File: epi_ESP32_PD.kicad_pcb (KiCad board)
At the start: 4 copper layers, 12.7 x 49.6 mm, 62 parts, among them J1 Conn_01x08, J2 USB_C_Receptacle_USB2.0, J3 Conn_01x08, J4 Conn_01x02, J6 Conn_Coaxial_Small, J7 Conn_02x03, J8 Conn_01x03, Q1 Q_PMOS_GDS, Q2 Q_NMOS_GDS, Q3 Q_NMOS_GDS, Q4 Q_NMOS_GDS, Q5 Q_NMOS_GDS, Q6 Q_NMOS_GDS, SW1 SW_MEC_5G, SW2 SW_MEC_5G, U1 ESP32-C3, U2 MIC5219-3.3YM5, U5 AP63205WU, Y1 Crystal

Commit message: made it pretty
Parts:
- removed DRILL1, DRILL2: NPTH, DIY:NPTH
- added JP4: Jumper, Jumper:SolderJumper-2_P1.3mm_Open_RoundedPad1.0x1.5mm, B.Cu at (103.9, 55.1)
- J2: footprint diy:USB-C MC-314C-4P16_V2 (2023_01_13 17_48_46 UTC) -> Connector_USB:USB_C_Receptacle_G-Switch_GT-USB-7010ASV
- moved JP3 1.65 mm to (101.9, 44.4), turned to 180 degrees
- moved JP2 0.89 mm to (101.9, 47.5), turned to 0 degrees
- moved J4 0.51 mm to (108.3, 48.9)
- moved R13 0.41 mm to (109.0, 79.3), turned to -90 degrees
- moved JP1 0.40 mm to (101.9, 50.6), turned to 0 degrees
- moved SW1 0.30 mm to (102.1, 61.5)
- moved R11 0.22 mm to (106.1, 75.0)
- moved C7 0.20 mm to (104.9, 68.5)
- moved J2 0.17 mm to (104.2, 36.4)
- moved C14 0.10 mm to (106.3, 53.1)
- moved R7 0.10 mm to (100.0, 45.4)
- moved C8 0.10 mm to (100.0, 43.2)
- moved R15 0.10 mm to (100.0, 46.4)
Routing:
- net +5V: track 60.0 -> 64.9 mm
- net Net-(JP2-B): track 12.7 -> 9.06 mm, vias 2 -> 1
- net IO2: track 23.4 -> 20.7 mm
- net Net-(JP1-B): track 14.5 -> 12.7 mm, vias 2 -> 1
- net Net-(JP3-A): track 3.20 -> 4.95 mm
- net D-: track 32.3 -> 33.7 mm
- net VIN: track 26.2 -> 26.9 mm
- net IO6: track 25.1 -> 24.5 mm
- net GND: vias 20 -> 24
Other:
- board size 12.7 x 49.6 mm -> 12.7 x 49.9 mm
- board text added: "20"
- board text added: "21"
- board text added: "3,3V"
- board text added: "5V"
- board text added: "B"
- board text added: "GND"
- board text added: "IO2-5V"
- board text added: "IO3-5V"
- board text added: "VOUT"
- board text added: "W"
- board text removed: "10"
- board text removed: "3,3v"
- board text removed: "RX/20"
- board text removed: "TX/21"

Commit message: finishing touches
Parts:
- removed C8: 1µF, Capacitor_SMD:C_0805_2012Metric
- added D1: D_Small, Diode_SMD:D_SOD-128, F.Cu at (104.7, 44.2)
- added REF**: Fiducial_0.5mm_Mask1.5mm, Fiducial:Fiducial_0.5mm_Mask1.5mm, F.Cu at (100.3, 36.5)
- J4: value Conn_01x02 -> Conn_01x01; footprint Connector_PinHeader_2.54mm:PinHeader_1x02_P2.54mm_Vertical -> TestPoint:TestPoint_Pad_3.0x3.0mm
- moved RV2 7.02 mm to (102.3, 44.3)
- moved RV3 7.02 mm to (102.3, 42.4), turned to -90 degrees
- moved R3 7.01 mm to (102.3, 46.2)
- moved U3 6.98 mm to (98.1, 44.3)
- moved J4 6.44 mm to (101.9, 49.0), turned to 180 degrees
- moved R1 4.30 mm to (103.9, 47.9)
- moved R8 4.30 mm to (103.9, 48.9)
- moved JP4 4.16 mm to (100.0, 53.7)
- moved J8 3.99 mm to (94.0, 71.1)
- moved Q1 3.94 mm to (103.9, 72.6)
- moved Q3 3.94 mm to (96.9, 72.6)
- moved Q5 3.94 mm to (100.4, 72.6)
- moved R12 3.94 mm to (95.4, 81.5)
- moved R13 3.94 mm to (105.1, 79.7), turned to 90 degrees
- moved R4 3.94 mm to (103.3, 70.0)
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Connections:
- J2 pad A4: VIN -> /PD
- J2 pad A9: VIN -> /PD
- J2 pad B4: VIN -> /PD
- J2 pad B9: VIN -> /PD
- JP1 pad 1: VIN -> +5V
- JP2 pad 1: VIN -> +5V
- JP3 pad 2: VIN -> +5V
- R1 pad 1: Net-(U3-VDD) -> +5V
- R1 pad 2: VIN -> /PD
- R7 pad 1: VIN -> /PD
- U3 pad 1: Net-(U3-VDD) -> +5V
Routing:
- net VIN: track 26.9 -> 6.54 mm, vias 9 -> 5
- net /PD: track 0.00 -> 19.6 mm, vias 0 -> 7
- net +5V: track 64.9 -> 81.4 mm
- net Net-(J2-CC1): track 5.30 -> 13.0 mm
- net EN: track 31.6 -> 26.0 mm
- net Net-(JP3-A): track 4.95 -> 9.07 mm, vias 1 -> 2
- net GND: track 0.00 -> 3.85 mm
- net D-: track 33.7 -> 30.7 mm, vias 3 -> 2
- net Net-(J2-CC2): track 2.05 -> 4.62 mm
- net D+: track 35.1 -> 33.2 mm, vias 3 -> 2
- net Net-(U3-VDD): track 1.82 -> 0.00 mm
- net Net-(JP2-B): track 9.06 -> 7.66 mm
- net +3.3V: track 28.5 -> 29.8 mm, vias 8 -> 9
- net Net-(U3-VBUS): track 3.75 -> 4.48 mm
- net IO2: track 20.7 -> 21.4 mm
- added copper zone on B.Cu, net /PD
- added copper zone on F.Cu, net /PD
- added copper zone on In2.Cu, net /PD
- removed copper zone on In2.Cu, net VIN
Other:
- board text added: "5V only"
- board text added: "IO0"

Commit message: little fix
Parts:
- added C8: 1µF, Capacitor_SMD:C_0402_1005Metric, F.Cu at (101.5, 48.1)
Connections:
- JP1 pad 1: +5V -> +3.3V
- JP2 pad 1: +5V -> +3.3V
- JP3 pad 2: +5V -> +3.3V
- R1 pad 1: +5V -> +3.3V
- U3 pad 1: +5V -> +3.3V
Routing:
- net +5V: track 81.4 -> 63.5 mm
- net +3.3V: track 29.8 -> 43.6 mm, vias 9 -> 11
- net GND: track 3.85 -> 4.58 mm

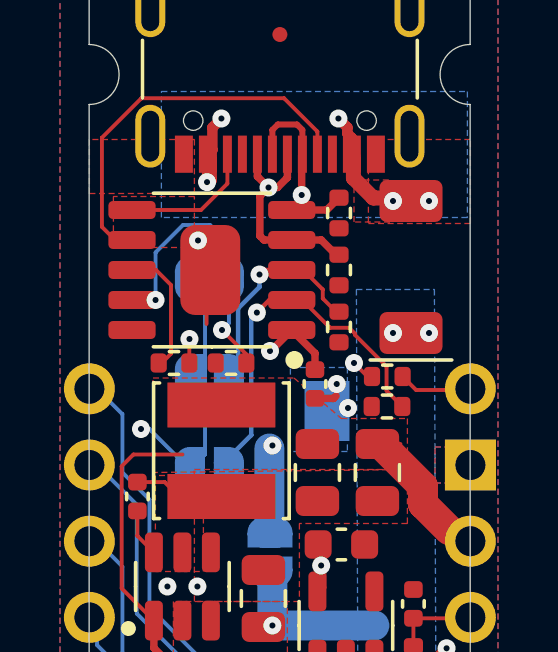
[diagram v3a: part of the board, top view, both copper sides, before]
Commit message: added a couple debugging jumpers
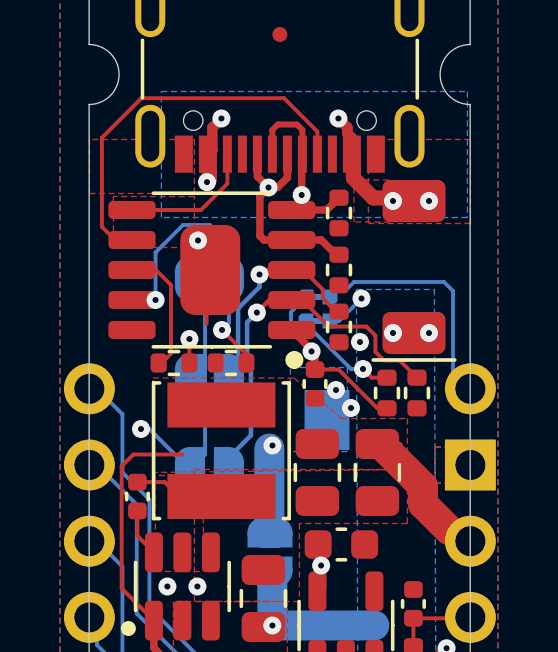
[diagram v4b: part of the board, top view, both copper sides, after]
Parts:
- added JP5: Jumper, Jumper:SolderJumper-2_P1.3mm_Bridged_RoundedPad1.0x1.5mm, B.Cu at (101.6, 46.0)
- added JP6: Jumper, Jumper:SolderJumper-2_P1.3mm_Bridged_RoundedPad1.0x1.5mm, B.Cu at (101.6, 45.2)
- moved R8 1.10 mm to (104.9, 48.4), turned to 90 degrees
- moved R1 0.55 mm to (103.9, 48.4), turned to 90 degrees
- moved J4 0.30 mm to (101.9, 49.3)
- moved D1 0.10 mm to (104.8, 44.2)
- turned C8 to -90 degrees
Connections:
- C8 pad 1: GND -> Net-(JP6-B)
- C8 pad 2: +3.3V -> GND
- R1 pad 1: +3.3V -> Net-(JP6-B)
- R1 pad 2: /PD -> Net-(JP5-A)
- U3 pad 1: +3.3V -> Net-(JP6-B)
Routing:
- net Net-(JP6-B): track 0.00 -> 7.08 mm, vias 0 -> 1
- net Net-(JP5-A): track 0.00 -> 3.54 mm, vias 0 -> 1
- net +3.3V: track 43.6 -> 46.6 mm, vias 11 -> 10
- net /PD: track 19.6 -> 18.0 mm
- net GND: track 4.58 -> 3.85 mm, vias 24 -> 25

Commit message: mix
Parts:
- added D2: D_Zener, Diode_SMD:D_SOD-323, B.Cu at (102.0, 43.2)
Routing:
- net Net-(D2-K): track 7.08 -> 9.18 mm
- net IO2_5V: track 15.3 -> 15.8 mm
- net GND: vias 25 -> 30
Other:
- board size 12.7 x 49.9 mm -> 22.7 x 54.9 mm

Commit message: revision
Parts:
- removed C12, C5: 1µF, Capacitor_SMD:C_0402_1005Metric
- removed C14: 22µF, Capacitor_SMD:C_0603_1608Metric
- removed C2, C7: 100nF, Capacitor_SMD:C_0402_1005Metric
- removed C3, C4, C6: TBD, Capacitor_SMD:C_0402_1005Metric
- removed D2: D_Zener, Diode_SMD:D_SOD-323
- removed J3: Conn_01x08, Connector_PinHeader_2.54mm:PinHeader_1x08_P2.54mm_Vertical
- removed J6: Conn_Coaxial_Small, Connector_Coaxial:U.FL_Molex_MCRF_73412-0110_Vertical
- removed JP5, JP6: Jumper, Jumper:SolderJumper-2_P1.3mm_Bridged_RoundedPad1.0x1.5mm
- removed L1: TBD, Resistor_SMD:R_0402_1005Metric
- removed Q5, Q6: Q_NMOS_GDS, Package_TO_SOT_SMD:SOT-23-3
- removed R2: 22Ω, Resistor_SMD:R_0402_1005Metric
- removed R4, R5: 10K, Resistor_SMD:R_0402_1005Metric
- removed RV2: Varistor, Resistor_SMD:R_0402_1005Metric
- removed SW1: SW_MEC_5G, DIY:R-668048
- removed Y1: Crystal, Crystal:Crystal_SMD_2016-4Pin_2.0x1.6mm
- added J5: Conn_01x09, Connector_PinHeader_2.54mm:PinHeader_1x09_P2.54mm_Vertical, F.Cu at (106.7, 48.3)
- C1: value 100nF -> 1µF
- Q1: value Q_PMOS_GDS -> Q_NMOS_GSD; footprint Package_TO_SOT_SMD:SOT-23-3 -> Package_TO_SOT_SMD:SOT-23
- Q2, Q3, Q4: value Q_NMOS_GDS -> Q_NMOS_GSD; footprint Package_TO_SOT_SMD:SOT-23-3 -> Package_TO_SOT_SMD:SOT-23
- R1: value 1K -> TBD
- R15, R3, R8: value 10K -> 1K
- U1: value ESP32-C3 -> ESP32-C3-MINI-1; footprint Package_DFN_QFN:QFN-32-1EP_5x5mm_P0.5mm_EP3.45x3.45mm -> PCM_Espressif:ESP32-C3-MINI-1
- moved J7 20.1 mm to (104.5, 60.2)
- moved R14 19.7 mm to (96.8, 59.9), turned to 0 degrees
- moved R12 16.9 mm to (98.5, 64.8), turned to 0 degrees
- moved REF** 16.3 mm to (104.8, 44.2)
- moved C1 14.9 mm to (101.5, 54.7)
- moved J8 13.5 mm to (97.8, 84.1), turned to 90 degrees
- moved U1 11.2 mm to (102.5, 76.4), turned to -90 degrees
- moved Q2 11.1 mm to (96.8, 66.2)
- moved R13 11.0 mm to (104.1, 68.7), turned to 180 degrees
- moved Q4 10.5 mm to (103.6, 66.2)
- moved Q3 10.3 mm to (96.8, 62.3), turned to -90 degrees
- moved R11 8.55 mm to (96.8, 68.7)
- moved R10 7.39 mm to (101.9, 68.7), turned to 180 degrees
- moved Q1 7.38 mm to (100.2, 66.2)
- moved REF** 7.37 mm to (98.6, 80.3)
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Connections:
- C8 pad 1: Net-(D2-K) -> +3.3V
- D1 pad 2: /PD -> PD
- J2 pad A4: /PD -> PD
- J2 pad A9: /PD -> PD
- J2 pad B4: /PD -> PD
- J2 pad B9: /PD -> PD
- J7 pad 1: VOUT -> +5V
- J7 pad 3: B -> IO2_5V
- J7 pad 4: IO2_5V -> B
- J7 pad 5: W -> IO3_5V
- J7 pad 6: IO3_5V -> W
- Q1 pad 1: Net-(Q1-G) -> +3.3V
- Q1 pad 2: VOUT -> IO2
- Q1 pad 3: VIN -> IO2_5V
- Q2 pad 1: IO6 -> +3.3V
- Q2 pad 2: B -> IO3
- Q2 pad 3: GND -> IO3_5V
- Q3 pad 1: +3.3V -> IO7
- Q3 pad 2: IO2_5V -> GND
- Q3 pad 3: IO2 -> W
- Q4 pad 1: +3.3V -> IO6
- Q4 pad 2: IO3_5V -> GND
- Q4 pad 3: IO3 -> B
- R1 pad 1: Net-(D2-K) -> +3.3V
- R1 pad 2: Net-(JP5-A) -> PD
- R13 pad 1: IO6 -> GND
- R13 pad 2: +3.3V -> IO6
- R14 pad 1: IO7 -> GND
- R14 pad 2: +3.3V -> IO7
- R7 pad 1: /PD -> PD
- RV3 pad 1: D- -> PD
- U1 pad 1: Net-(U1-LNA_IN) -> GND
- U1 pad 10: IO5 -> unconnected-(U1-NC-Pad10)
- U1 pad 11: +3.3V -> GND
- U1 pad 12: IO6 -> IO0
- U1 pad 13: IO7 -> IO1
- U1 pad 14: IO8 -> GND
- U1 pad 15: BOOT -> unconnected-(U1-NC-Pad15)
- U1 pad 17: +3.3V -> unconnected-(U1-NC-Pad17)
- U1 pad 18: Net-(U1-VDD_SPI/GPIO11) -> IO4
- U1 pad 19: unconnected-(U1-SPIHD/GPIO12-Pad19) -> IO5
- U1 pad 2: +3.3V -> GND
- U1 pad 20: unconnected-(U1-SPIWP/GPIO13-Pad20) -> IO6
- U1 pad 21: unconnected-(U1-SPICS0/GPIO14-Pad21) -> IO7
- U1 pad 22: unconnected-(U1-SPICLK/GPIO15-Pad22) -> IO8
- U1 pad 23: unconnected-(U1-SPID/GPIO16-Pad23) -> BOOT
- U1 pad 25: D- -> unconnected-(U1-NC-Pad25)
- U1 pad 26: D+ -> D-
- U1 pad 27: U0RXD -> D+
- U1 pad 28: U0TXD -> unconnected-(U1-NC-Pad28)
- U1 pad 29: Net-(U1-XTAL_N) -> unconnected-(U1-NC-Pad29)
- U1 pad 30: Net-(U1-XTAL_P) -> U0RXD
- U1 pad 31: +3.3V -> U0TXD
- U1 pad 32: +3.3V -> unconnected-(U1-NC-Pad32)
- U1 pad 33: GND -> unconnected-(U1-NC-Pad33)
- U1 pad 4: IO0 -> unconnected-(U1-NC-Pad4)
- U1 pad 5: IO1 -> IO2
- U1 pad 6: IO2 -> IO3
- U1 pad 7: EN -> unconnected-(U1-NC-Pad7)
- U1 pad 8: IO3 -> EN
- U1 pad 9: IO4 -> unconnected-(U1-NC-Pad9)
- U3 pad 1: Net-(D2-K) -> +3.3V
- U3 pad 4: D+ -> unconnected-(U3-DP-Pad4)
- U3 pad 5: D- -> unconnected-(U3-DM-Pad5)
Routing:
- net +5V: track 63.7 -> 35.5 mm, vias 2 -> 4
- net U0TXD: track 18.2 -> 40.4 mm
- net U0RXD: track 17.2 -> 37.5 mm
- net /PD: track 18.0 -> 0.00 mm, vias 7 -> 0
- net D-: track 30.9 -> 48.8 mm
- net IO3: track 33.6 -> 15.7 mm, vias 1 -> 0
- net +3.3V: track 46.6 -> 30.0 mm, vias 10 -> 7
- net PD: track 0.00 -> 16.3 mm, vias 0 -> 8
- net IO8: track 7.96 -> 22.4 mm
- net D+: track 33.2 -> 46.8 mm
- net IO10: track 10.1 -> 22.1 mm, vias 2 -> 1
- net IO7: track 22.7 -> 33.5 mm, vias 2 -> 1
- net Net-(D2-K): track 9.18 -> 0.00 mm, vias 1 -> 0
- net Net-(U1-XTAL_N): track 7.49 -> 0.00 mm
- net IO0: track 29.6 -> 36.8 mm
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- added copper zone on In2.Cu, net +5V
- added copper zone on B.Cu, net PD
- added copper zone on F.Cu, net PD
- added copper zone on In2.Cu, net PD
- removed copper zone on B.Cu, net /PD
- removed copper zone on F.Cu, net /PD
- removed copper zone on In2.Cu, net /PD
- removed copper zone on B.Cu, net VOUT
- removed copper zone on F.Cu, net VOUT
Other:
- board size 22.7 x 54.9 mm -> 12.7 x 49.8 mm
- board text added: "Epi-C3-PD V1,1"
- board text added: "IO2-5"
- board text added: "IO3-5"
- board text added: "R"
- board text removed: "8"
- board text removed: "BOOT"
- board text removed: "Epi-C3-PD"
- board text removed: "IO2-5V"
- board text removed: "IO3-5V"
- board text removed: "RST"
- board text removed: "VOUT"
